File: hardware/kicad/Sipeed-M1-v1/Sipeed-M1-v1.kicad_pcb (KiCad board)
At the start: 2 copper layers, 165 parts, among them IC1 TROPIC01_chip, J1 USB_C_, J2 JST Connector, J3 Conn_02x20_Odd_Even, J4 Conn_01x09_Pin, J5 Conn_02x03_Odd_Even, Q2 FS8205A, SW1 SW_Push, SW10 SW_Push, SW11 SW_Push, SW12 SW_Push, SW13 SW_Push, SW14 SW_Push, SW15 SW_Push, SW16 SW_Push, SW2 SW_Push, SW3 SW_Push, SW4 SW_Push, SW5 SW_Push, SW6 SW_Push, SW7 SW_Push, SW8 SW_Push, SW9 SW_Push, U1 Sipeed-M1, U2 ESP32-S3-WROOM-1U-N8R8, U3 PAM2401YPADJ, U4 TPS63070RNMR, U5 MCP23017_SO, U6 BQ29700DSER, U7 USBLC6-2SC6, U8 MCP73871

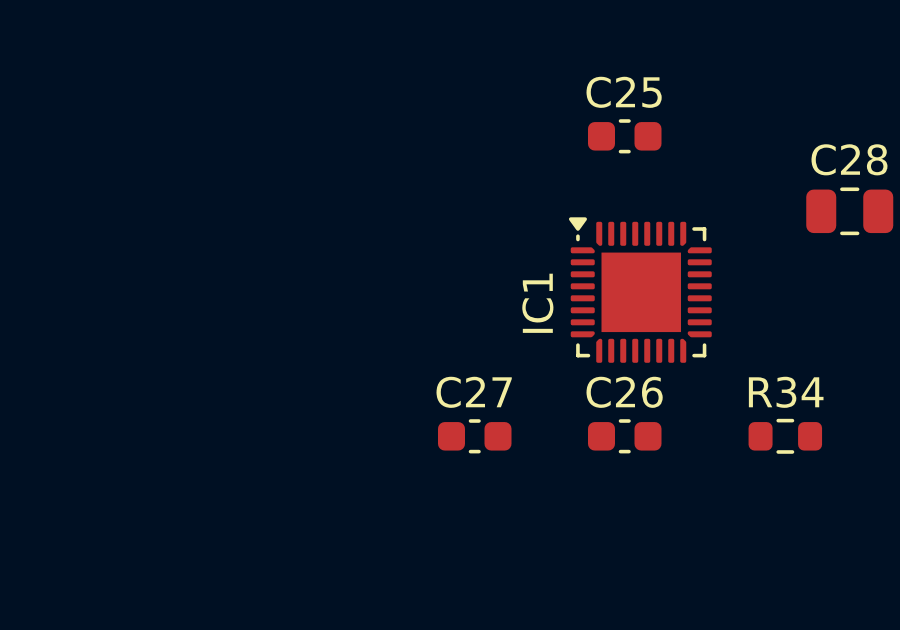
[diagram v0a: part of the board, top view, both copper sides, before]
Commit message: cleared some errors for pcb import from schematic(update pcb)
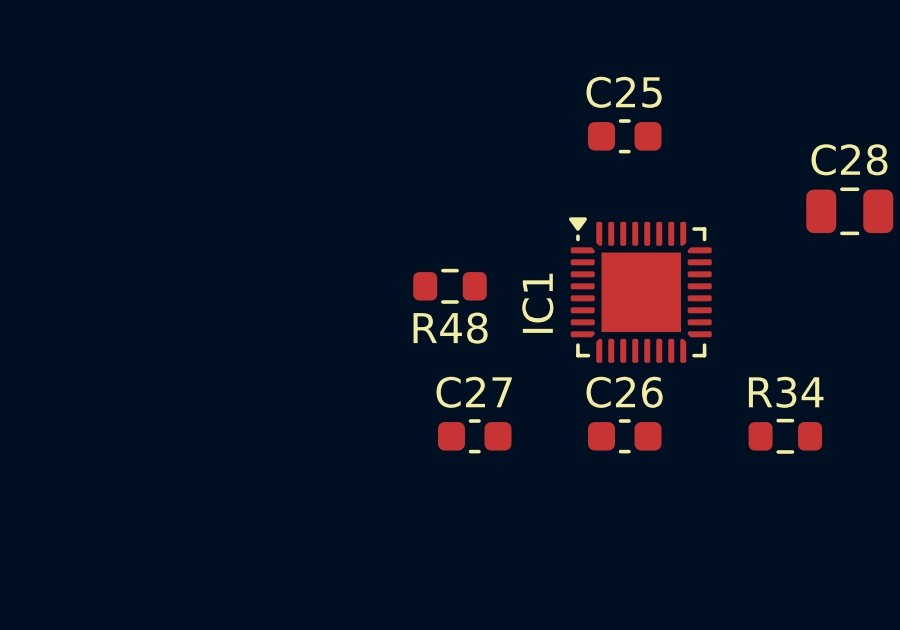
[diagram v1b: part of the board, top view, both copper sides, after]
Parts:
- added R48: 47k, Resistor_SMD:R_0603_1608Metric, F.Cu at (124.2, 40.0)
- IC1: footprint _M1_FP_lib:QFN-32-1EP_4x4mm_P0.4mm_EP2.65x2.65mm TROPIC01 -> _M1_FP_lib:TROPIC01 QFN-32-1EP_4x4mm_P0.4mm_EP2.65x2.65mm
- U2: footprint _M1_FP_lib:XCVR_ESP32-S3-WROOM-1U-N8R8 -> _M1_FP_lib:XCVR_ESP32-S3-WROOM-1U-N8R8-NU
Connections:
- IC1 pad 1: +3.3V_SYS -> unconnected-(IC1-VCC-Pad1)
- IC1 pad 15: (no net) -> unconnected-(IC1-NC-Pad15)
- IC1 pad 16: (no net) -> unconnected-(IC1-NC-Pad16)
- IC1 pad 25: (no net) -> unconnected-(IC1-NC-Pad25)
- IC1 pad 32: (no net) -> unconnected-(IC1-NC-Pad32)

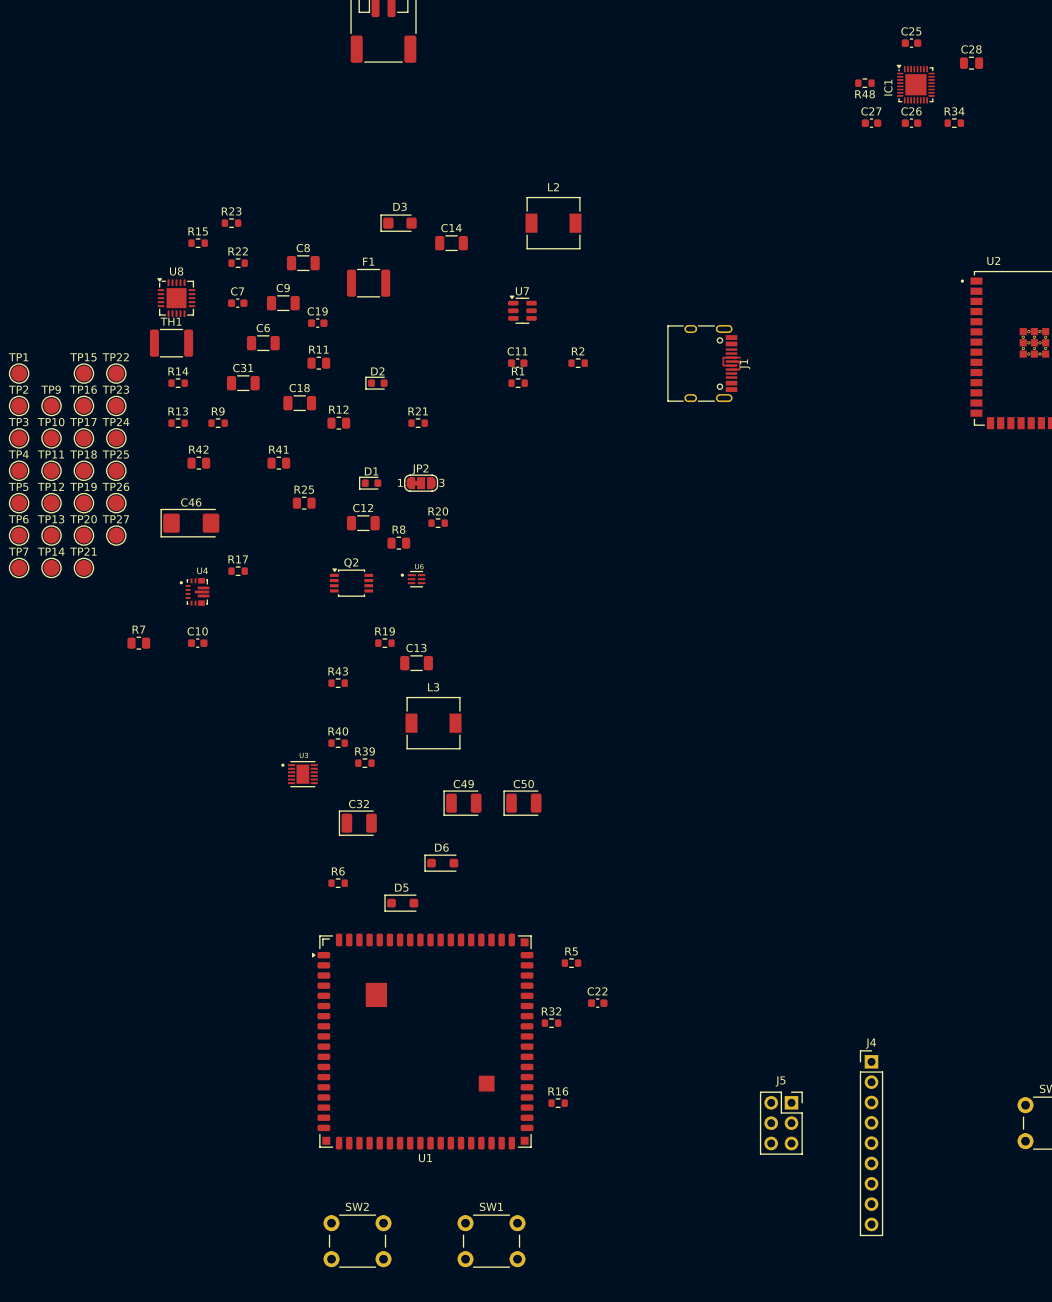
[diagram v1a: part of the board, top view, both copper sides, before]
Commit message: Added FPs and sorted the pcb board
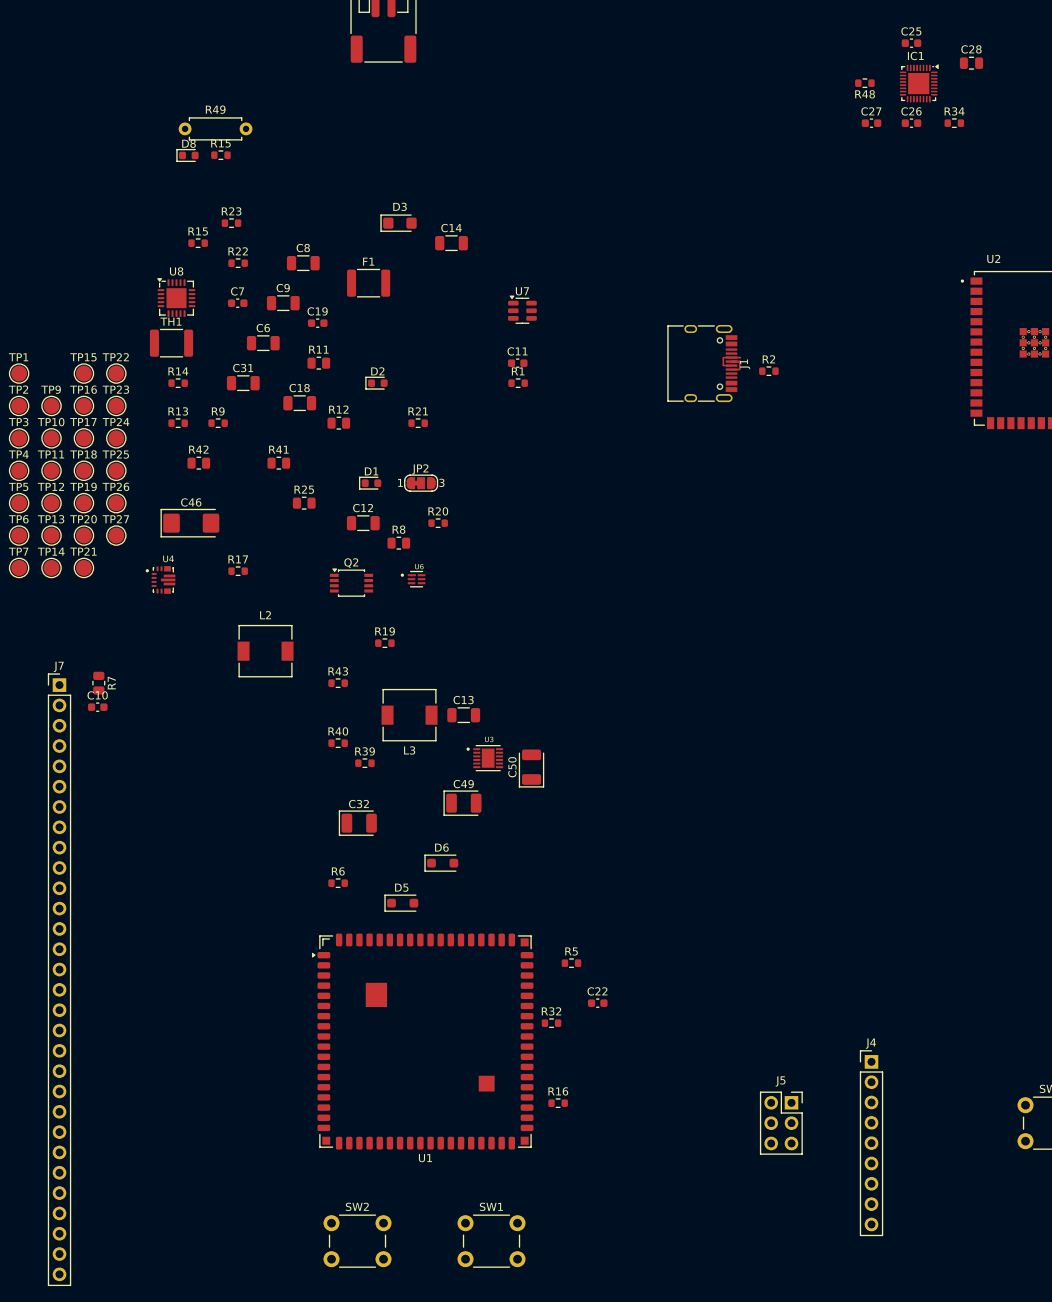
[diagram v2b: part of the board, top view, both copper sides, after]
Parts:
- added D8: LED_BL, LED_SMD:LED_0603_1608Metric, F.Cu at (39.7, 49.0)
- added J7: Conn_01x30_Pin, Connector_PinHeader_2.54mm:PinHeader_1x30_P2.54mm_Vertical, F.Cu at (23.5, 115.2)
- added R15: 430, Resistor_SMD:R_0603_1608Metric, F.Cu at (43.7, 49.0)
- added R49: 1K, Resistor_THT:R_Axial_DIN0207_L6.3mm_D2.5mm_P7.62mm_Horizontal, F.Cu at (39.2, 45.7)
- C13: value 10uF -> 4.7uF
- C31: value 22uF -> 4.7uF
- IC1: footprint _M1_FP_lib:TROPIC01 QFN-32-1EP_4x4mm_P0.4mm_EP2.65x2.65mm -> _M1_FP_lib:TROPIC_QFN-32-1EP_4x4mm_P0.4mm_EP2.65x2.65mm
- R13, R14: value 1k -> 430
- TH1: value Therm._NTC -> 10k
- U2: footprint _M1_FP_lib:XCVR_ESP32-S3-WROOM-1U-N8R8-NU -> _M1_FP_lib:ESP32-S3-WROOM-1U
- U3: footprint _M1_FP_lib:SON45P300X300X63-13N PAM2401 -> _M1_FP_lib:PAM2401_SON45P300X300X63-13N
- U6: footprint _M1_FP_lib:BQ29700DSER SON50P150X150X80-6N -> _M1_FP_lib:BQ29700_SON50P150X150X80-6N
- moved L2 64.5 mm to (49.2, 111.0)
- moved R2 23.9 mm to (112.2, 76.0)
- moved U3 23.2 mm to (77.1, 124.4)
- moved C10 14.8 mm to (28.3, 118.0)
- moved C13 8.78 mm to (74.0, 119.0)
- moved R7 7.07 mm to (28.4, 115.0), turned to -90 degrees
- moved C50 4.60 mm to (82.5, 125.5), turned to 90 degrees
- moved U4 4.51 mm to (36.5, 102.1)
- moved L3 3.16 mm to (67.2, 119.0), turned to 180 degrees
- moved IC1 0.38 mm to (130.9, 40.0), turned to -90 degrees
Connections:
- C11 pad 1: GND -> VBUS
- C11 pad 2: VBUS -> GND
- D1 pad 1: GND -> Net-(D1-K)
- D1 pad 2: Net-(D1-A) -> VBUS
- D2 pad 1: GND -> Net-(D2-K)
- D2 pad 2: Net-(D2-A) -> VBUS
- IC1 pad 1: unconnected-(IC1-VCC-Pad1) -> +3.3V_SYS
- J1 pad A6: /USB_D+ -> Net-(J1-D+-PadA6)
- J1 pad B6: /USB_D+ -> Net-(J1-D+-PadA6)
- R13 pad 2: Net-(D1-A) -> Net-(D1-K)
- R14 pad 2: Net-(D2-A) -> Net-(D2-K)
- U1 pad 10: unconnected-(U1-IO9-Pad10) -> /M1_IO9
- U1 pad 11: unconnected-(U1-IO10-Pad11) -> /M1_IO10
- U1 pad 12: unconnected-(U1-IO11-Pad12) -> /M1_IO11
- U1 pad 18: unconnected-(U1-IO17-Pad18) -> /M1_IO17
- U1 pad 19: unconnected-(U1-IO18-Pad19) -> /M1_MIC_BCK
- U1 pad 20: unconnected-(U1-IO19-Pad20) -> /M1_MIC_WS
- U1 pad 21: unconnected-(U1-IO20-Pad21) -> /M1_MIC_DAT3
- U1 pad 22: unconnected-(U1-IO21-Pad22) -> /M1_MIC_DAT2
- U1 pad 23: unconnected-(U1-IO22-Pad23) -> /M1_MIC_DAT1
- U1 pad 24: unconnected-(U1-IO23-Pad24) -> /M1_MIC_DAT0
- U1 pad 28: /SPI_SCK -> /SPI_SCLK
- U1 pad 31: unconnected-(U1-IO30-Pad31) -> /M1_MIC0_WS
- U1 pad 32: unconnected-(U1-IO31-Pad32) -> /M1_MIC0_DATA
- U1 pad 33: unconnected-(U1-IO32-Pad33) -> /M1_MIC0_BCK
- U1 pad 34: unconnected-(U1-IO33-Pad34) -> /M1_I2S_WS
- U1 pad 35: unconnected-(U1-IO34-Pad35) -> /M1_I2S_DA
- U1 pad 36: unconnected-(U1-IO35-Pad36) -> /M1_I2S_BCK
- U1 pad 41: /TX_M1 -> unconnected-(U1-IO40-Pad41)
- U1 pad 42: /RX_M1 -> unconnected-(U1-IO41-Pad42)
- U1 pad 5: Net-(U1-IO4/ISP_Rx) -> /TX_M1
- U1 pad 6: Net-(U1-IO5/ISP_Tx) -> /RX_M1
- U1 pad 7: unconnected-(U1-IO6-Pad7) -> /M1_IO6
- U1 pad 8: unconnected-(U1-IO7-Pad8) -> /M1_IO7
- U1 pad 9: unconnected-(U1-IO8-Pad9) -> /M1_IO8
- U7 pad 3: /USB_D+ -> Net-(J1-D+-PadA6)
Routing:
- net Net-(J1-D+-PadA6): track 0.00 -> 4.12 mm
- net /USB_D+: track 4.12 -> 0.00 mm

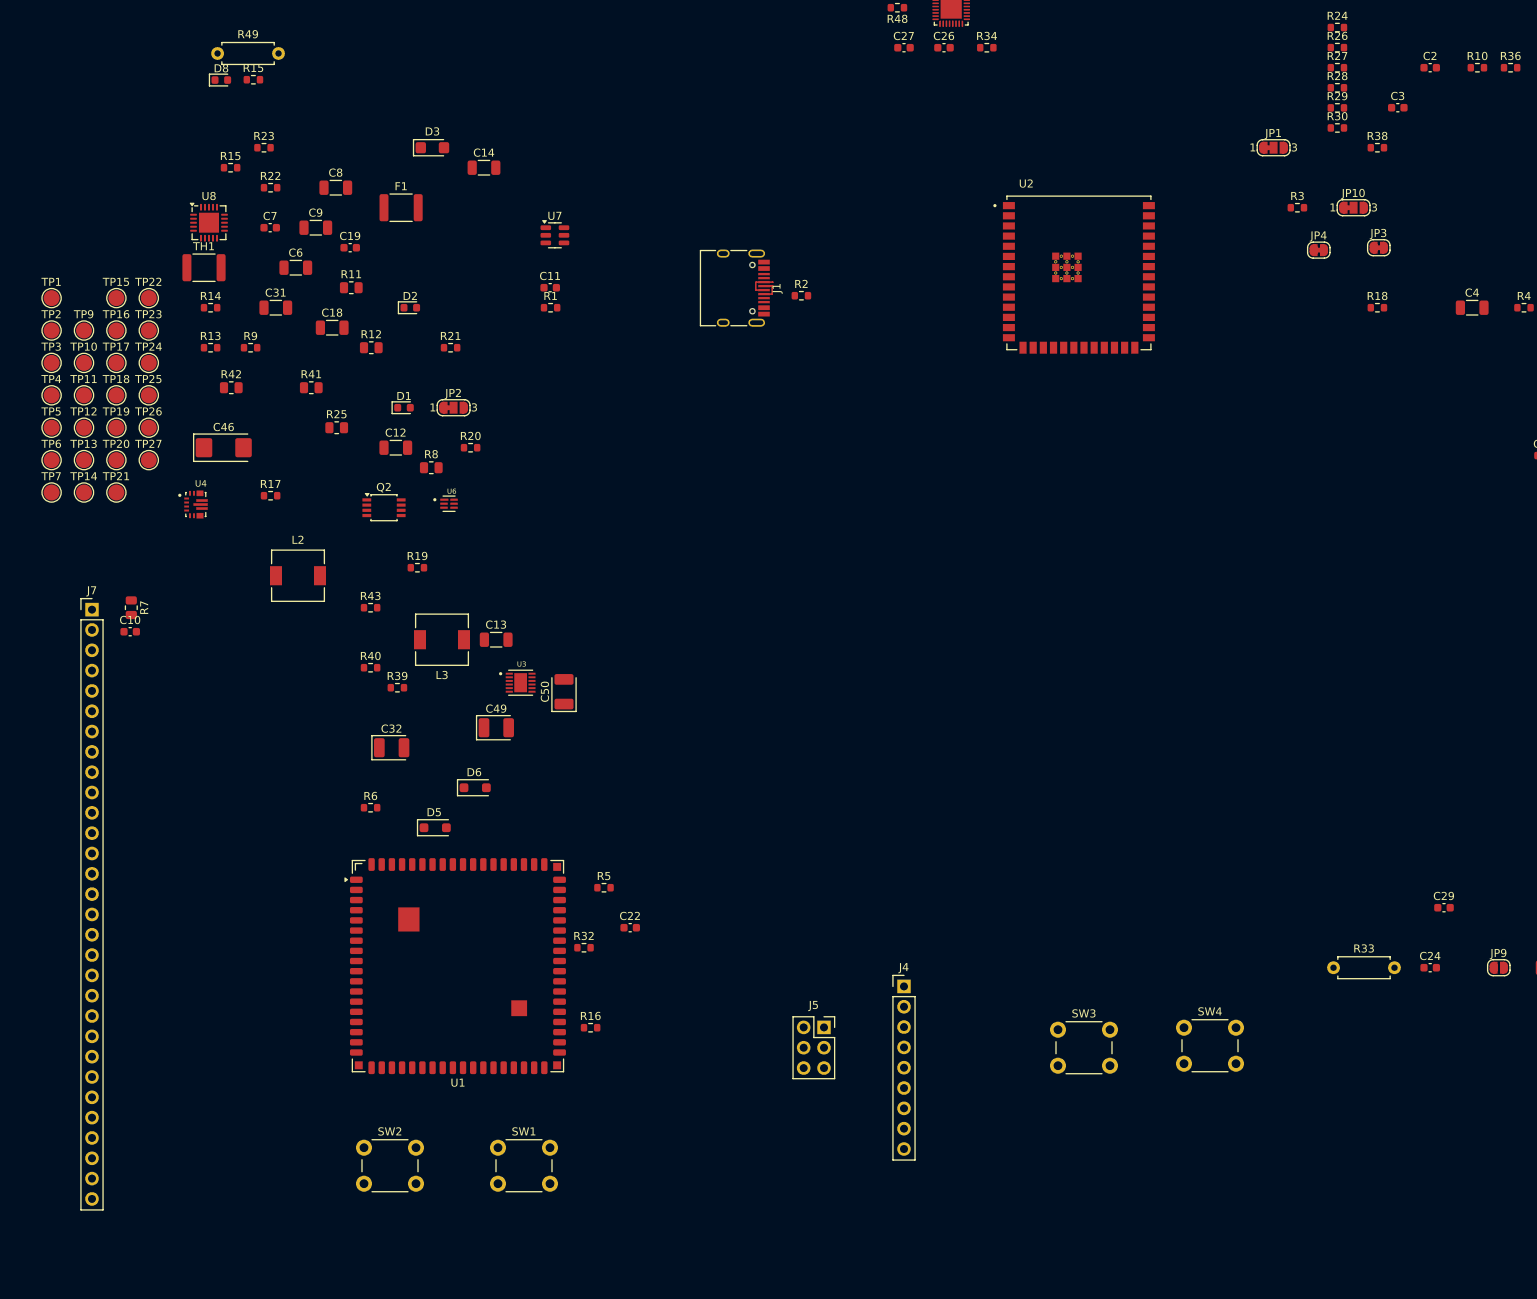
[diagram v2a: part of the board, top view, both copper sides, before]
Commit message: updated pcb, added 3v3 and 1v8 net to m1, checked proper deletion of battery prot IC as lipos have their own
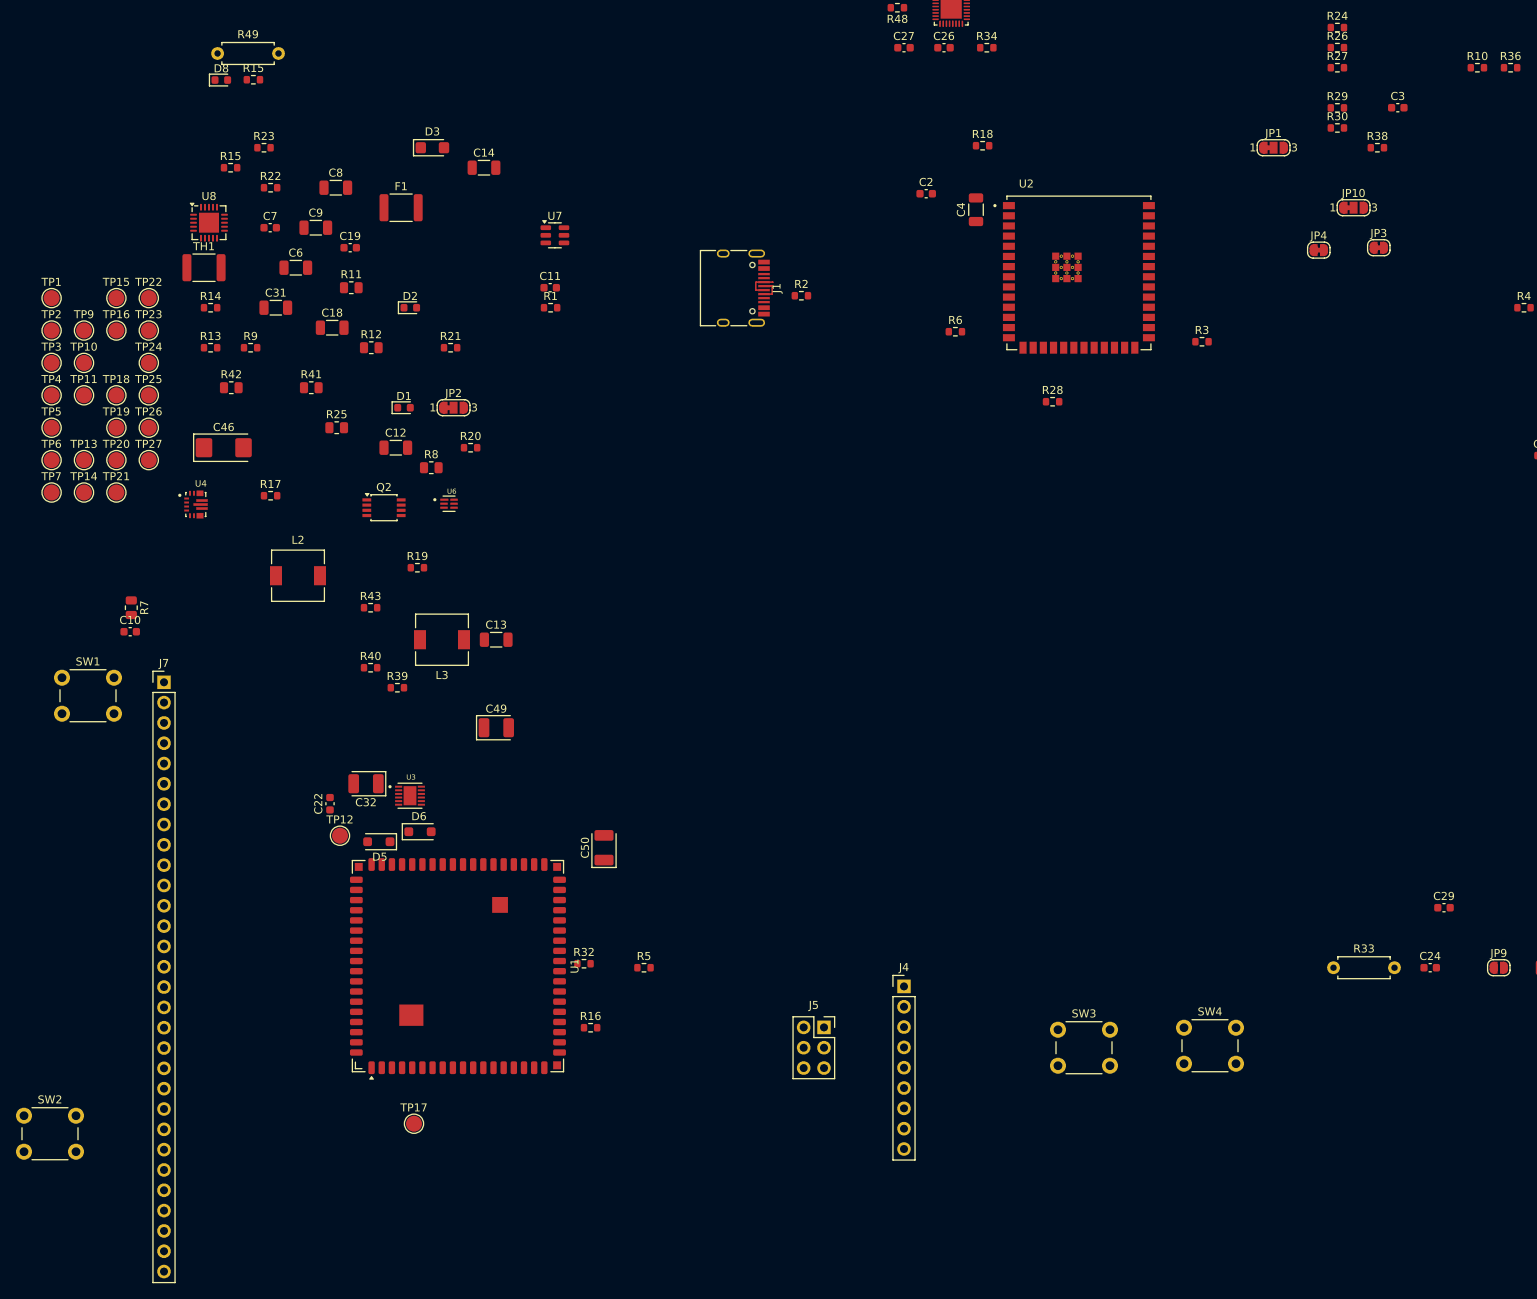
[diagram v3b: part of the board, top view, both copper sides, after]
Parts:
- moved TP17 102.1 mm to (63.8, 179.5)
- moved R6 94.3 mm to (131.4, 80.5)
- moved SW1 80.1 mm to (19.8, 123.8)
- moved C2 64.9 mm to (127.8, 63.2)
- moved C4 63.2 mm to (134.0, 65.2), turned to 90 degrees
- moved TP12 60.2 mm to (54.5, 143.5)
- moved R18 53.3 mm to (134.8, 57.2)
- moved R28 53.0 mm to (143.6, 89.2)
- moved SW2 42.7 mm to (15.0, 178.5)
- moved C22 40.6 mm to (53.2, 139.5), turned to 90 degrees
- moved R3 20.6 mm to (162.2, 81.8)
- moved C50 20.1 mm to (87.5, 145.0)
- moved U3 19.8 mm to (63.2, 138.5)
- moved J7 12.8 mm to (32.5, 124.3)
- moved R5 11.2 mm to (92.5, 160.0)
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
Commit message: Removed Protection IC from project
removed battery protection IC BQ29700DSER from our project, as the common lipos have their own anyways onboard.
updated and removed some other symbols and footprints too (removed the BQ29,
changed output pin to power output at 3v3 boost conv., removed unused)
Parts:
- removed C14: 10uF, Capacitor_SMD:C_1206_3216Metric
- removed C46: 100uF 10V Tant, Capacitor_Tantalum_SMD:CP_EIA-6032-28_Kemet-C
- removed Q2: FS8205A, _M1_FP_lib:FS8205A TSSOP-8_3x3mm_P0.65mm
- removed R17, R20: 100 O, Resistor_SMD:R_0603_1608Metric
- removed R19, R21: 100k, Resistor_SMD:R_0603_1608Metric
- removed TP2: TP_DOUT, TestPoint:TestPoint_Pad_D2.0mm
- removed TP3: TP_COUT, TestPoint:TestPoint_Pad_D2.0mm
- U2: footprint _M1_FP_lib:ESP32-S3-WROOM-1U -> _M1_FP_lib:XCVR_ESP32-S3-WROOM-1U-N8R8-NU
- moved TP10 87.7 mm to (108.0, 64.8)
- moved TP1 73.2 mm to (72.5, 27.0)
- moved C15 63.5 mm to (241.7, 52.5)
- moved F1 55.0 mm to (114.1, 83.0)
- moved D3 48.3 mm to (113.8, 64.8)
- moved R41 47.9 mm to (64.4, 133.5)
- moved C11 45.2 mm to (37.8, 61.0)
- moved R8 35.3 mm to (31.5, 105.2)
- moved U7 34.8 mm to (116.1, 70.8)
- moved R1 31.3 mm to (111.8, 72.5)
- moved JP7 28.3 mm to (235.8, 74.5), turned to -90 degrees
- moved JP6 28.1 mm to (237.2, 69.5), turned to 90 degrees
- moved JP8 26.2 mm to (238.2, 81.2), turned to -90 degrees
- moved C16 16.8 mm to (242.8, 89.8)
- moved R35 13.3 mm to (254.9, 76.0)
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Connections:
- C1 pad 1: /CELL- -> GND
- J1 pad A6: Net-(J1-D+-PadA6) -> /USB_D+
- J1 pad B6: Net-(J1-D+-PadA6) -> /USB_D+
- J2 pad 2: /CELL- -> GND
- R16 pad 1: +3.3V_SYS -> /3V3_M1
- R5 pad 1: +3.3V_SYS -> /1V8_M1
- U1 pad 53: unconnected-(U1-1V8-Pad53) -> /1V8_M1
- U1 pad 54: unconnected-(U1-3V3-Pad54) -> /3V3_M1
- U7 pad 3: Net-(J1-D+-PadA6) -> /USB_D+
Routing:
- net Net-(J1-D+-PadA6): track 4.12 -> 0.00 mm
- net /USB_D+: track 0.00 -> 4.12 mm
